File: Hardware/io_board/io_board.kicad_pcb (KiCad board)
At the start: 2 copper layers, 127 x 36.2 mm, 86 parts, among them J1 Valves, J10 ADC_VDIV, J11 12V IN, J12 CAN, J13 AS5047, J14 SWD, J15 CAN, J2 Valves, J3 Valves, J4 Steering, J5 Steering, J6 Limit SW, J7 Limit SW, J8 ADC_IO, J9 ADC_VDIV, Q1 Q_NMOS_GSD, Q10 Q_NMOS_GSD, Q11 Q_NMOS_GSD, Q12 Q_NMOS_GSD, Q13 Q_NMOS_GSD, Q2 Q_NMOS_GSD, Q3 Q_NMOS_GSD, Q4 Q_NMOS_GSD, Q5 Q_NMOS_GSD, Q6 Q_NMOS_GSD, Q7 Q_NMOS_GSD, Q8 Q_NMOS_GSD, Q9 Q_NMOS_GSD, U1 AZ1117-3.3, U2 TJA1051TK-3, U3 STM32F405RGTx, Y1 8M

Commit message: added some text to the IO board
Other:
- board text added: "IO Controller 2020 V1_0 MACTRAC"

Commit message: Updated io board silkscreen
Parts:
- added G***: LOGO, io_board:mactrac, F.Cu at (105.8, 76.3)
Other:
- board text added: "5V"
- board text added: "CANH"
- board text added: "CANL"
- board text added: "CS"
- board text added: "MISO"
- board text added: "MOSI"
- board text added: "NRST"
- board text added: "SCK"
- board text added: "SWCLK"
- board text added: "SWDIO"
- board text added: "VCC"

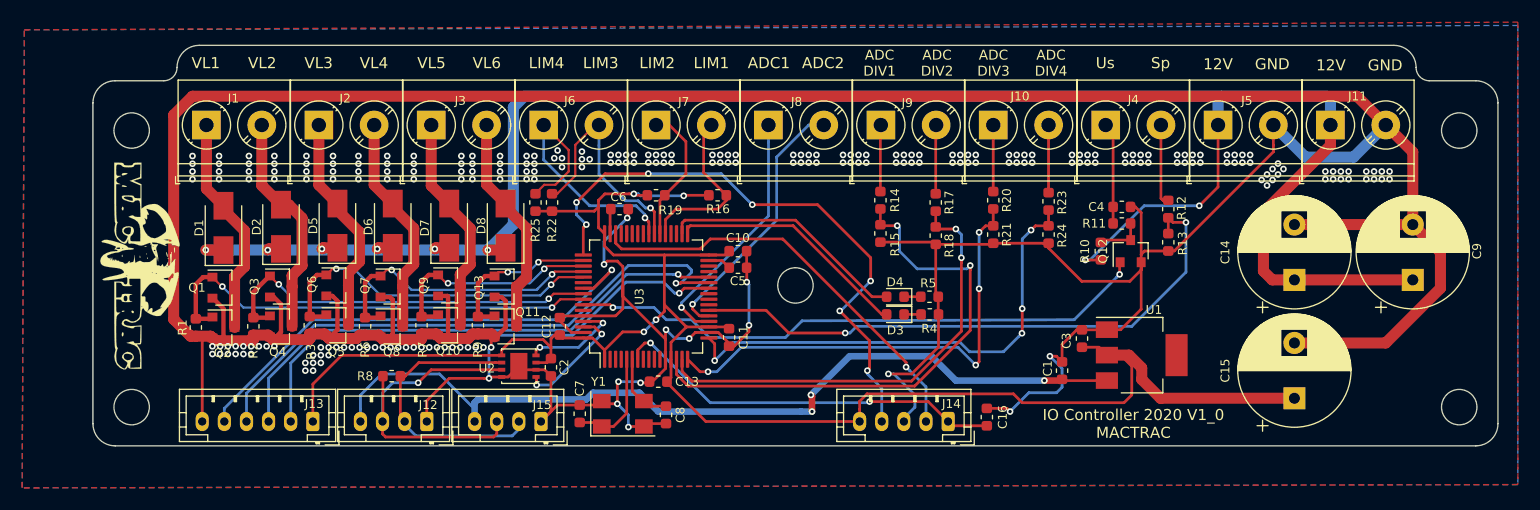
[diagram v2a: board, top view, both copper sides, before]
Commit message: Added io_board fw and fixed io_board hw bug
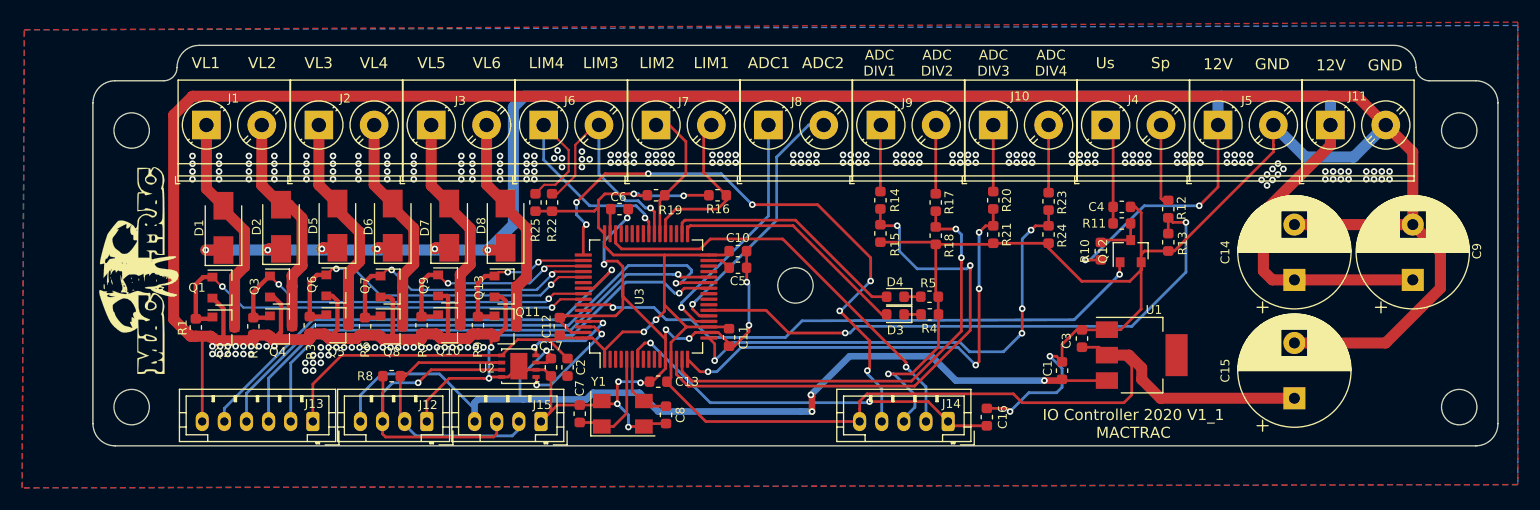
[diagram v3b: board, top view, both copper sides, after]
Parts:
- added C17: 2.2u, Capacitor_SMD:C_0603_1608Metric, F.Cu at (142.9, 85.4)
- moved C2 1.50 mm to (144.4, 85.4)
- moved G*** 0.36 mm to (105.6, 76.6), turned to 90 degrees
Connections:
- net /mcu/CAN_RX renamed /CAN_RX
- net /mcu/CAN_TX renamed /CAN_TX
- net /mcu/LED_GREEN renamed /LED_GREEN
- net /mcu/LED_RED renamed /LED_RED
- U2 pad 3: VCC -> +5V
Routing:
- net +5V: track 80.0 -> 87.9 mm, vias 3 -> 4
- net VCC: track 168.8 -> 167.4 mm
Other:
- board text added: "IO Controller 2020 V1_1 MACTRAC"
- board text removed: "IO Controller 2020 V1_0 MACTRAC"
